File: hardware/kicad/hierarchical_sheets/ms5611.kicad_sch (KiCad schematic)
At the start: 2 parts, among them U4 MS5611-01BA

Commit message: massive comment upload
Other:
- note added: "Comments: - There needs to be a ~{CS} pullup resistor between the ~{CS} pin and 3.3v. Make this resistor 10k. The only purpose of this resistor is to ensure that the chip stays inactive while the microcontroller is being initially programmed since during programming the chip will be unable to hold the various ~{CS} lines high. A higher value reistor is less likely to cause problems during normal 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"
- moved on the sheet: C6, U4

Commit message: fixed barometer board haha - ben
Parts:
- added R22: 10K, symbol Device:R
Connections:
- net +3.3V: now also R22.1
- net ~{CS}: now also R22.2
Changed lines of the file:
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@@
     (company "Missouri S&T Rocket Design Team")
   )
+  (junction (at 40.005 92.075) (diameter 0) (color 0 0 0 0)
+  )
   (junction (at 106.045 75.565) (diameter 0) (color 0 0 0 0)
   )
@@
     (stroke (width 0) (type default))
   )
+  (wire (pts (xy 40.005 64.135) (xy 40.005 73.66))
+    (stroke (width 0) (type default))
+  )
   (wire (pts (xy 66.675 84.455) (xy 78.105 84.455))
     (stroke (width 0) (type default))
@@
     (stroke (width 0) (type default))
   )
-  (wire (pts (xy 66.675 92.075) (xy 78.105 92.075))
+  (wire (pts (xy 30.48 92.075) (xy 40.005 92.075))
     (stroke (width 0) (type default))
   )
@@
     (stroke (width 0) (type default))
   )
+  (wire (pts (xy 40.005 92.075) (xy 78.105 92.075))
+    (stroke (width 0) (type default))
+  )
   (wire (pts (xy 88.265 100.965) (xy 106.045 100.965))
     (stroke (width 0) (type default))
@@
   )
   (wire (pts (xy 106.045 92.075) (xy 106.045 100.965))
+    (stroke (width 0) (type default))
+  )
+  (wire (pts (xy 40.005 81.28) (xy 40.005 92.075))
     (stroke (width 0) (type default))
   )
@@
     (effects (font (size 1.27 1.27)) (justify left bottom))
   )
-  (hierarchical_label "~{CS}" (shape output) (at 66.675 92.075 180) (fields_autoplaced)
+  (hierarchical_label "~{CS}" (shape output) (at 30.48 92.075 180) (fields_autoplaced)
     (effects (font (size 1.27 1.27)) (justify right))
   )
@@
         (path "/54cce219-8b98-4e71-96c4-f9ee784aa3bc/01e59dc5-0a98-4437-b4f9-a1305517a629"
           (reference "#PWR07") (unit 1)
+        )
+      )
+    )
+  )
+  (symbol (lib_id "Device:R") (at 40.005 77.47 0) (unit 1)
+    (in_bom yes) (on_board yes) (dnp no) (fields_autoplaced)
+    (property "Reference" "R22" (at 42.545 76.835 0)
+      (effects (font (size 1.27 1.27)) (justify left))
+    )
+    (property "Value" "10K" (at 42.545 79.375 0)
+      (effects (font (size 1.27 1.27)) (justify left))
+    )
+    (property "Footprint" "" (at 38.227 77.47 90)
+      (effects (font (size 1.27 1.27)) hide)
+    )
+    (property "Datasheet" "~" (at 40.005 77.47 0)
+      (effects (font (size 1.27 1.27)) hide)
+    )
+    (pin "1")
+    (pin "2")
+    (instances
+      (project "FC"
+        (path "/54cce219-8b98-4e71-96c4-f9ee784aa3bc/01e59dc5-0a98-4437-b4f9-a1305517a629"
+          (reference "R22") (unit 1)
         )
       )
@@
         )
       )
+    )
+  )
+  (symbol (lib_id "power:+3.3V") (at 40.005 64.135 0) (unit 1)
+    (in_bom yes) (on_board yes) (dnp no)
+    (property "Reference" "#PWR01" (at 40.005 67.945 0)
+      (effects (font (size 1.27 1.27)) hide)
+    )
+    (property "Value" "+3.3V" (at 40.005 60.325 0)
+      (effects (font (size 1.27 1.27)))
+    )
+    (property "Footprint" "" (at 40.005 64.135 0)
+      (effects (font (size 1.27 1.27)) hide)
+    )
+    (property "Datasheet" "" (at 40.005 64.135 0)
+      (effects (font (size 1.27 1.27)) hide)
+    )
+    (pin "1")
+    (instances
+      (project "FC"
+        (path "/54cce219-8b98-4e71-96c4-f9ee784aa3bc/aac89dea-c005-40db-a234-32c8ed41f1e5"
+          (reference "#PWR01") (unit 1)
+        )
+        (path "/54cce219-8b98-4e71-96c4-f9ee784aa3bc/01e59dc5-0a98-4437-b4f9-a1305517a629"
+          (reference "#PWR028") (unit 1)
+        )
+      )

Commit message: Current Max
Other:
- note added: "Max Current: 1.4 mA"
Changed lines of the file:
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@@
     (stroke (width 0) (type default))
+  )
+  (text "Max Current: 1.4 mA" (at 152.4 69.85 0)
+    (effects (font (size 1.27 1.27)) (justify left bottom))
   )
   (text "Comments:\n\n- There needs to be a ~{CS} pullup resistor between the ~{CS} pin and 3.3v. Make this\n	resistor 10k. The only purpose of this resistor is to ensure that the chip \n	stays inactive while the microcontroller is being initially programmed since\n	during programming the chip will be unable to hold the various ~{CS} lines high. \n	A higher value reistor is less likely to cause problems during normal operation. \n\n			-Seth"

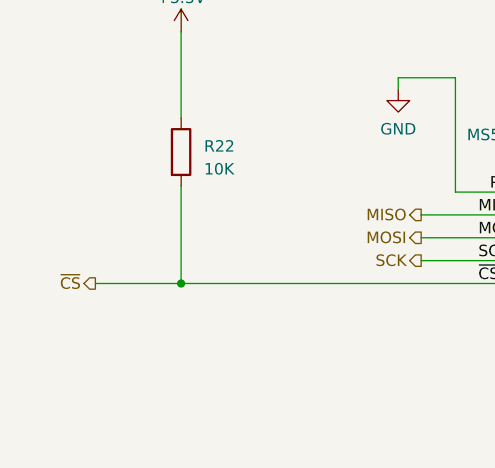
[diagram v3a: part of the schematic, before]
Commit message: started linking together FC, changed cs directions
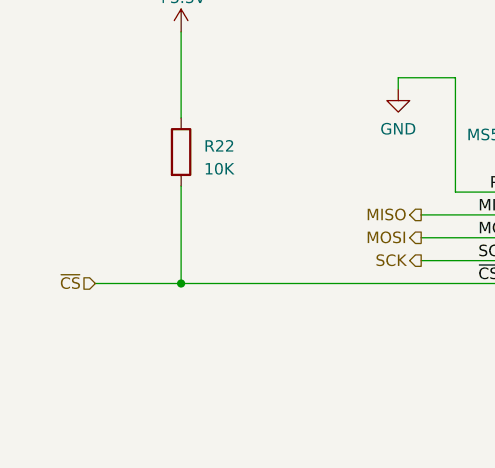
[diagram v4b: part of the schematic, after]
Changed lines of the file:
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@@
     (effects (font (size 1.27 1.27)) (justify left bottom))
   )
-  (hierarchical_label "~{CS}" (shape output) (at 30.48 92.075 180) (fields_autoplaced)
+  (hierarchical_label "~{CS}" (shape input) (at 30.48 92.075 180) (fields_autoplaced)
     (effects (font (size 1.27 1.27)) (justify right))
   )

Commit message: added power and checked schematics
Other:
- note removed: "Comments: - There needs to be a ~{CS} pullup resistor between the ~{CS} pin and 3.3v. Make this resistor 10k. The only purpose of this resistor is to ensure that the chip stays inactive while the microcontroller is being initially programmed since during programming the chip will be unable to hold the various ~{CS} lines high. A higher value reistor is less likely to cause problems during normal 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"
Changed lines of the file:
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@@
     (stroke (width 0) (type default))
   )
-  (text "Max Current: 1.4 mA" (at 152.4 69.85 0)
+  (text "Max Current: 1.4 mA" (at 14.605 201.295 0)
     (effects (font (size 1.27 1.27)) (justify left bottom))
   )
-  (text "Comments:\n\n- There needs to be a ~{CS} pullup resistor between the ~{CS} pin and 3.3v. Make this\n	resistor 10k. The only purpose of this resistor is to ensure that the chip \n	stays inactive while the microcontroller is being initially programmed since\n	during programming the chip will be unable to hold the various ~{CS} lines high. \n	A higher value reistor is less likely to cause problems during normal operation. \n\n			-Seth"
-    (at 120.015 48.26 0)
-    (effects (font (size 2 2) (thickness 0.4) bold (color 255 48 0 1)) (justify left bottom))
-  )
   (label "MOSI" (at 73.025 86.995 0) (fields_autoplaced)
